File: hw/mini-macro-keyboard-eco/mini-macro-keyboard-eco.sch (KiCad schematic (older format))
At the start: 39 parts, among them J0 USB_B_Micro, J1 SWD, SW0 SW_SPDT, SW1 SW_1, SW2 SW_2, SW3 SW_3, SW4 RESET, SW5 SW_SPDT, SW6 SW_SPDT, U1 USBLC6-2SC6, U2 XC6206P322MR, U3 STM32F070F6Px, Y1 16 MHz

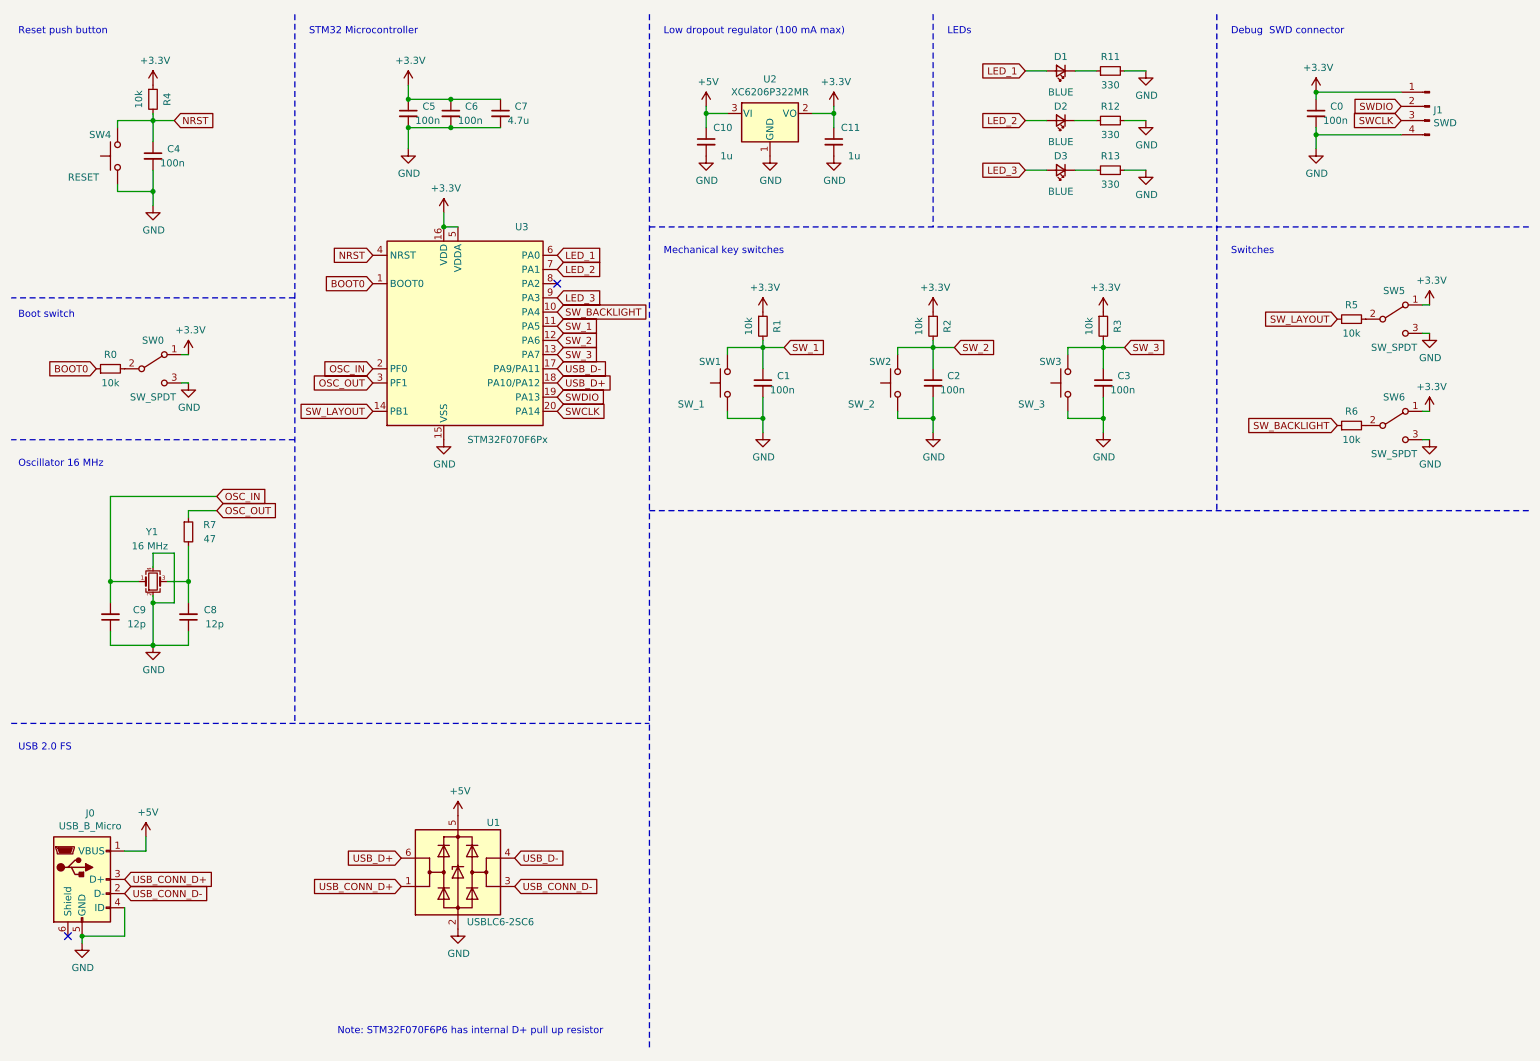
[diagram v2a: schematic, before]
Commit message: style(hw): rename value fields
Signed-off-by: Ivan Kovalenko <s1ckretbox@gmail.com>
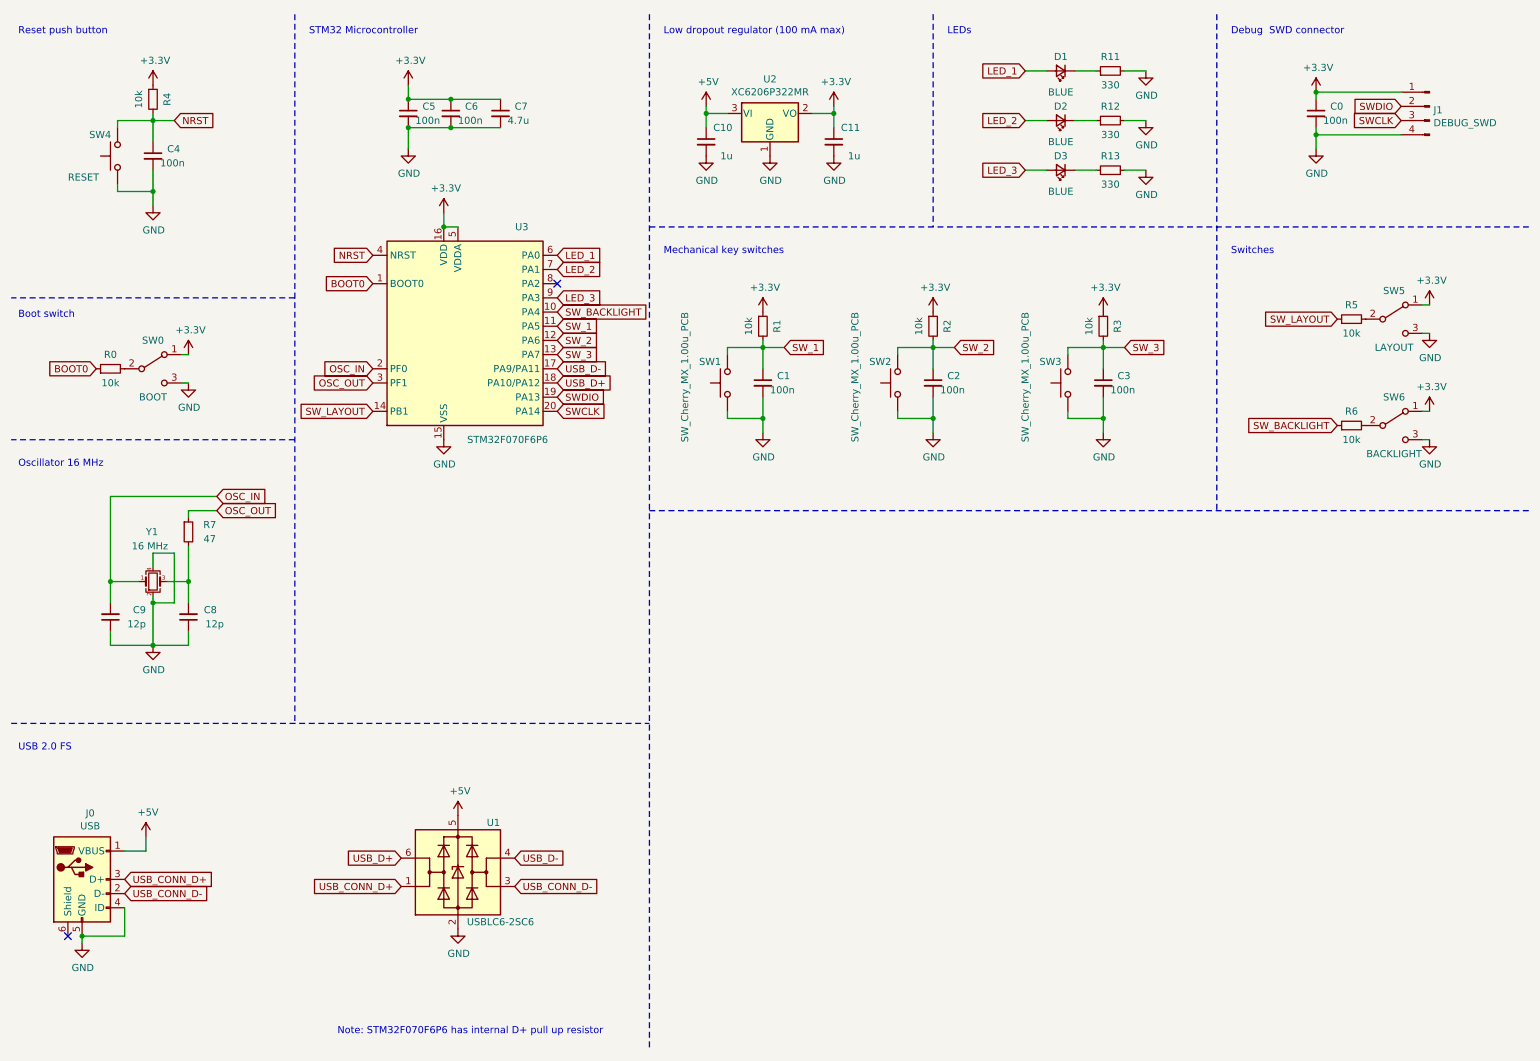
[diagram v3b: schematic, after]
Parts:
- J0: value USB_B_Micro -> USB
- J1: value SWD -> DEBUG_SWD
- SW0: value SW_SPDT -> BOOT
- SW1: value SW_1 -> SW_Cherry_MX_1.00u_PCB
- SW2: value SW_2 -> SW_Cherry_MX_1.00u_PCB
- SW3: value SW_3 -> SW_Cherry_MX_1.00u_PCB
- SW5: value SW_SPDT -> LAYOUT
- SW6: value SW_SPDT -> BACKLIGHT
- U3: value STM32F070F6Px -> STM32F070F6P6
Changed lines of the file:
@@
 P 1000 6600
 F 0 "J0" H 1057 7067 50  0000 C CNN
-F 1 "USB_B_Micro" H 1057 6976 50  0000 C CNN
+F 1 "USB" H 1057 6976 50  0000 C CNN
 F 2 "Connector_USB:USB_Micro-B_Molex-105017-0001" H 1150 6550 50  0001 C CNN
 F 3 "~" H 1150 6550 50  0001 C CNN
@@
 	5800 3200 5800 3350
 $Comp
-L mini-macro-keyboard-eco-rescue:SW_Push-Switch SW1
-U 1 1 5FFBA653
-P 5550 3100
-F 0 "SW1" V 5700 3300 50  0000 R CNN
-F 1 "SW_1" V 5400 3450 50  0000 R CNN
-F 2 "Button_Switch_Keyboard:SW_Cherry_MX_1.00u_PCB" H 5550 3300 50  0001 C CNN
-F 3 "~" H 5550 3300 50  0001 C CNN
-	1    5550 3100
-	0    -1   -1   0
-$EndComp
-$Comp
 L mini-macro-keyboard-eco-rescue:R_Small-Device R1
 U 1 1 5FFBA64D
@@
 	8200 3200 8200 3350
 $Comp
-L mini-macro-keyboard-eco-rescue:SW_Push-Switch SW3
-U 1 1 5FFC23E7
-P 7950 3100
-F 0 "SW3" V 8100 3300 50  0000 R CNN
-F 1 "SW_3" V 7800 3450 50  0000 R CNN
-F 2 "Button_Switch_Keyboard:SW_Cherry_MX_1.00u_PCB" H 7950 3300 50  0001 C CNN
-F 3 "~" H 7950 3300 50  0001 C CNN
-	1    7950 3100
-	0    -1   -1   0
-$EndComp
-$Comp
 L mini-macro-keyboard-eco-rescue:R_Small-Device R3
 U 1 1 5FFC23E1
@@
 Wire Wire Line
 	7000 3200 7000 3350
-$Comp
-L mini-macro-keyboard-eco-rescue:SW_Push-Switch SW2
-U 1 1 5FFBFB01
-P 6750 3100
-F 0 "SW2" V 6900 3300 50  0000 R CNN
-F 1 "SW_2" V 6600 3450 50  0000 R CNN
-F 2 "Button_Switch_Keyboard:SW_Cherry_MX_1.00u_PCB" H 6750 3300 50  0001 C CNN
-F 3 "~" H 6750 3300 50  0001 C CNN
-	1    6750 3100
-	0    -1   -1   0
-$EndComp
 $Comp
 L mini-macro-keyboard-eco-rescue:R_Small-Device R2
@@
 P 3750 2700
 F 0 "U3" H 4100 3400 50  0000 C CNN
-F 1 "STM32F070F6Px" H 4000 1900 50  0000 C CNN
+F 1 "STM32F070F6P6" H 4000 1900 50  0000 C CNN
 F 2 "Package_SO:TSSOP-20_4.4x6.5mm_P0.65mm" H 3150 2000 50  0001 R CNN
 F 3 "http://www.st.com/st-web-ui/static/active/en/resource/technical/document/datasheet/DM00141386.pdf" H 3750 2700 50  0001 C CNN
@@
 Wire Wire Line
 	3600 1300 3950 1300
-$Comp
-L mini-macro-keyboard-eco-rescue:Conn_01x04_Male-Connector J1
-U 1 1 5FFC7CBC
-P 10500 1150
-F 0 "J1" H 10472 1124 50  0000 R CNN
-F 1 "SWD" H 10472 1033 50  0000 R CNN
-F 2 "Connector_PinHeader_2.54mm:PinHeader_1x04_P2.54mm_Horizontal" H 10500 1150 50  0001 C CNN
-F 3 "~" H 10500 1150 50  0001 C CNN
-	1    10500 1150
-	-1   0    0    -1
-$EndComp
 Wire Wire Line
 	9700 1050 9700 1100
@@
 	1    0    0    -1
 $EndComp
-$Comp
-L mini-macro-keyboard-eco-rescue:SW_SPDT-Switch SW6
-U 1 1 6000BFDF
-P 10250 3400
-F 0 "SW6" H 10250 3600 50  0000 C CNN
-F 1 "SW_SPDT" H 10250 3200 50  0000 C CNN
-F 2 "Button_Switch_SMD:SW_SPDT_PCM12" H 10250 3400 50  0001 C CNN
-F 3 "~" H 10250 3400 50  0001 C CNN
-	1    10250 3400
-	1    0    0    -1
-$EndComp
 Wire Notes Line
 	9000 500  9000 4000
-$Comp
-L mini-macro-keyboard-eco-rescue:SW_SPDT-Switch SW5
-U 1 1 60009322
-P 10250 2650
-F 0 "SW5" H 10250 2850 50  0000 C CNN
-F 1 "SW_SPDT" H 10250 2450 50  0000 C CNN
-F 2 "Button_Switch_SMD:SW_SPDT_PCM12" H 10250 2650 50  0001 C CNN
-F 3 "~" H 10250 2650 50  0001 C CNN
-	1    10250 2650
-	1    0    0    -1
-$EndComp
 $Comp
 L mini-macro-keyboard-eco-rescue:GND-power #PWR0114
@@
 P 1500 3000
 F 0 "SW0" H 1500 3200 50  0000 C CNN
-F 1 "SW_SPDT" H 1500 2800 50  0000 C CNN
+F 1 "BOOT" H 1500 2800 50  0000 C CNN
 F 2 "Button_Switch_SMD:SW_SPDT_PCM12" H 1500 3000 50  0001 C CNN
 F 3 "~" H 1500 3000 50  0001 C CNN
@@
 Wire Wire Line
 	1200 3900 1200 4500
+$Comp
+L mini-macro-keyboard-eco-rescue:SW_SPDT-Switch SW6
+U 1 1 6000BFDF
+P 10250 3400
+F 0 "SW6" H 10250 3600 50  0000 C CNN
+F 1 "BACKLIGHT" H 10250 3200 50  0000 C CNN
+F 2 "Button_Switch_SMD:SW_SPDT_PCM12" H 10250 3400 50  0001 C CNN
+F 3 "~" H 10250 3400 50  0001 C CNN
+	1    10250 3400
+	1    0    0    -1
+$EndComp
+$Comp
+L mini-macro-keyboard-eco-rescue:Conn_01x04_Male-Connector J1
+U 1 1 5FFC7CBC
+P 10500 1150
+F 0 "J1" H 10472 1124 50  0000 R CNN
+F 1 "DEBUG_SWD" H 10472 1033 50  0000 R CNN
+F 2 "Connector_PinHeader_2.54mm:PinHeader_1x04_P2.54mm_Horizontal" H 10500 1150 50  0001 C CNN
+F 3 "~" H 10500 1150 50  0001 C CNN
+	1    10500 1150
+	-1   0    0    -1
+$EndComp
+$Comp
+L mini-macro-keyboard-eco-rescue:SW_Push-Switch SW3
+U 1 1 5FFC23E7
+P 7950 3100
+F 0 "SW3" V 8100 3300 50  0000 R CNN
+F 1 "SW_Cherry_MX_1.00u_PCB" H 8450 3400 50  0000 R CNN
+F 2 "Button_Switch_Keyboard:SW_Cherry_MX_1.00u_PCB" H 7950 3300 50  0001 C CNN
+F 3 "~" H 7950 3300 50  0001 C CNN
+	1    7950 3100
+	0    -1   -1   0
+$EndComp
+$Comp
+L mini-macro-keyboard-eco-rescue:SW_SPDT-Switch SW5
+U 1 1 60009322
+P 10250 2650
+F 0 "SW5" H 10250 2850 50  0000 C CNN
+F 1 "LAYOUT" H 10250 2450 50  0000 C CNN
+F 2 "Button_Switch_SMD:SW_SPDT_PCM12" H 10250 2650 50  0001 C CNN
+F 3 "~" H 10250 2650 50  0001 C CNN
+	1    10250 2650
+	1    0    0    -1
+$EndComp
+$Comp
+L mini-macro-keyboard-eco-rescue:SW_Push-Switch SW2
+U 1 1 5FFBFB01
+P 6750 3100
+F 0 "SW2" V 6900 3300 50  0000 R CNN
+F 1 "SW_Cherry_MX_1.00u_PCB" H 7250 3400 50  0000 R CNN
+F 2 "Button_Switch_Keyboard:SW_Cherry_MX_1.00u_PCB" H 6750 3300 50  0001 C CNN
+F 3 "~" H 6750 3300 50  0001 C CNN
+	1    6750 3100
+	0    -1   -1   0
+$EndComp
+$Comp
+L mini-macro-keyboard-eco-rescue:SW_Push-Switch SW1
+U 1 1 5FFBA653
+P 5550 3100
+F 0 "SW1" V 5700 3300 50  0000 R CNN
+F 1 "SW_Cherry_MX_1.00u_PCB" H 6050 3400 50  0000 R CNN
+F 2 "Button_Switch_Keyboard:SW_Cherry_MX_1.00u_PCB" H 5550 3300 50  0001 C CNN
+F 3 "~" H 5550 3300 50  0001 C CNN
+	1    5550 3100
+	0    -1   -1   0
+$EndComp
 $EndSCHEMATC
